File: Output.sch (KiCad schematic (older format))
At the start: 30 parts, among them Q1 2N7002, Q2 2N7002, Q3 AOD403, U7 74HC125

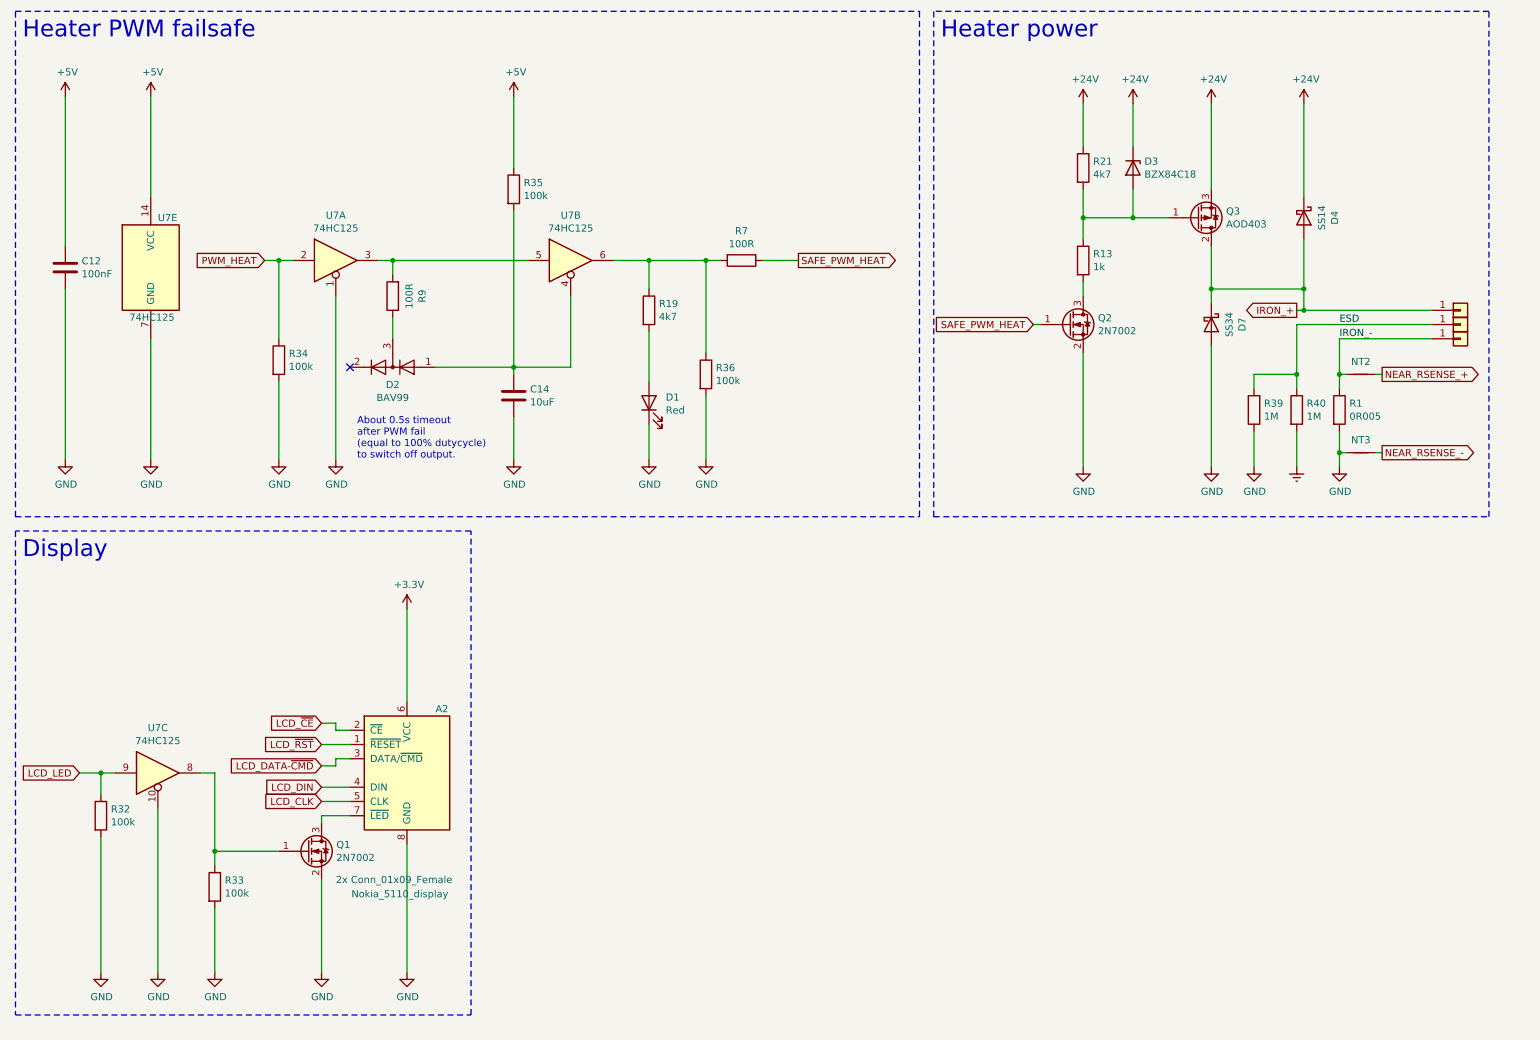
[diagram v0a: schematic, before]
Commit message: Added overheat protection that works, but very noisy.
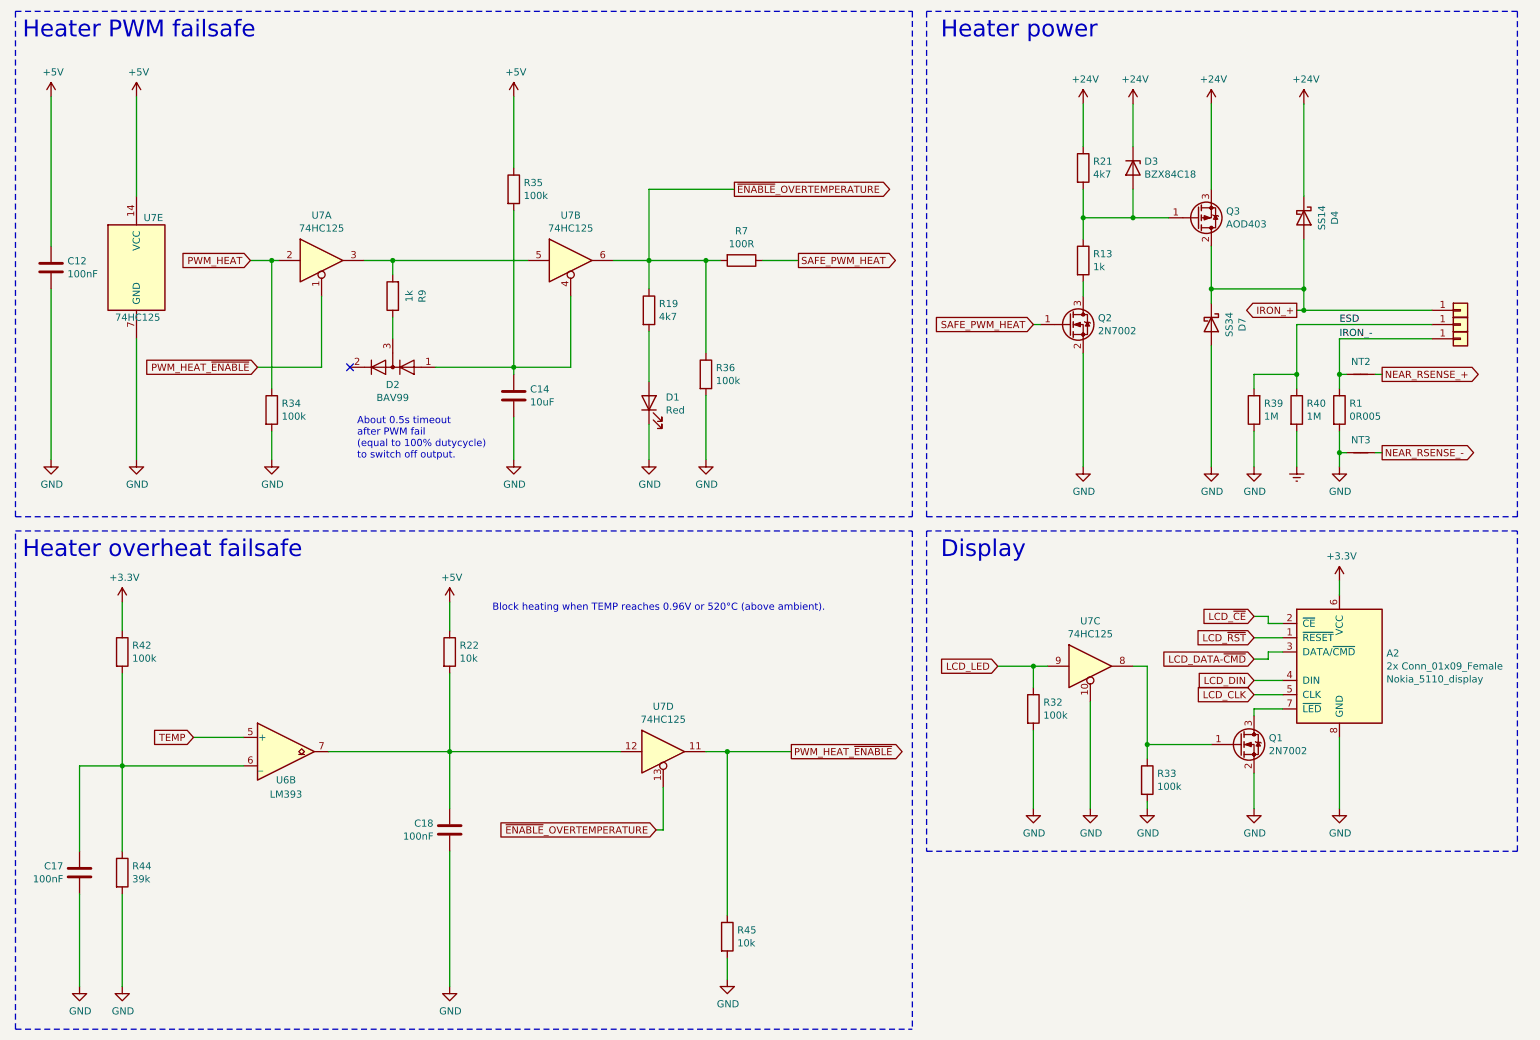
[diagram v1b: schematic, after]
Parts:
- added C17, C18: 100nF, Capacitor_SMD:C_0805_2012Metric_Pad1.18x1.45mm_HandSolder, symbol Device:C
- added R22, R45: 10k, Resistor_SMD:R_0805_2012Metric_Pad1.20x1.40mm_HandSolder, symbol Device:R
- added R42: 100k, Resistor_SMD:R_0805_2012Metric_Pad1.20x1.40mm_HandSolder, symbol Device:R
- added R44: 39k, Resistor_SMD:R_0805_2012Metric_Pad1.20x1.40mm_HandSolder, symbol Device:R
- added U6: LM393, Package_SO:SO-8_3.9x4.9mm_P1.27mm, symbol Comparator:LM393
- added unit 4 of U7
- R9: value 100R -> 1k
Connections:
- net +3V3: now also R42.1
- net +5V: now also R22.1
- net GND: now also C17.2, C18.2, R44.2, R45.2; no longer U7.1
- net ~ENABLE~_OVERTEMPERATURE: now reaches R19.1, R36.1, R7.2, U7.6
- net ~ENABLE~_OVERTEMPERATURE: now also U7.13
- new net: C17.1, R42.2, R44.1, U6.6 (_)
- new net: C18.1, R22.2, U6.7, U7.12
- new net PWM_HEAT_~ENABLE: R45.1, U7.1, U7.11
- new net TEMP: U6.5 (+)
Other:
- note added: "Block heating when TEMP reaches 0.96V or 520°C (above ambient).\n\n"
- note added: "Heater overheat failsafe"
- moved on the sheet: A2, C12, Q1, R32, R33, R34, U7A, U7C, U7E
